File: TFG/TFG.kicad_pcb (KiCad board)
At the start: 2 copper layers, 68.3 x 44.4 mm, 36 parts, among them IC1 MC74VHC1GT14DBVT1G, IC2 AMS1117-5.0, IC3 AMS1117-5.0, J1 Jack-DC, J2 CON-SMA-EDGE-SRP, J3 CON-SMA-EDGE-SRP, Q1 BFP420

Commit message: BOM Uploaded but SRD and Schottky diodes are pending
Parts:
- BFG135A1: footprint Package_TO_SOT_SMD:SOT-223 -> Package_TO_SOT_SMD:SOT-23
- moved BFG135A1 2.37 mm to (72.4, 74.3)
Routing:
- net Net-(BFG135A1-B): track 2.52 -> 7.57 mm
- net Net-(D1-K): track 15.6 -> 16.8 mm
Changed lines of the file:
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@@
 		(tags "capacitor")
 		(property "Reference" "C10"
-			(at 0 -1.43 360)
+			(at 0 -1.43 0)
 			(layer "F.SilkS")
 			(effects
@@
 		)
 		(property "Value" "C"
-			(at 0 1.43 360)
+			(at 0 1.43 0)
 			(layer "F.Fab")
 			(effects
@@
 		)
 		(fp_text user "${REFERENCE}"
-			(at 0 0 360)
+			(at 0 0 0)
 			(layer "F.Fab")
 			(effects
@@
 		(tags "capacitor")
 		(property "Reference" "C11"
-			(at 0 -1.43 360)
+			(at 0 -1.43 0)
 			(layer "F.SilkS")
 			(effects
@@
 		)
 		(property "Value" "0.1u"
-			(at 0 1.43 360)
+			(at 0 1.43 0)
 			(layer "F.Fab")
 			(effects
@@
 		)
 		(fp_text user "${REFERENCE}"
-			(at 0 0 360)
+			(at 0 0 0)
 			(layer "F.Fab")
 			(effects
@@
 		(tags "capacitor tantalum")
 		(property "Reference" "C6"
-			(at 0 -1.75 360)
+			(at 0 -1.75 0)
 			(layer "F.SilkS")
 			(effects
@@
 		)
 		(property "Value" "10u"
-			(at 0 1.75 360)
+			(at 0 1.75 0)
 			(layer "F.Fab")
 			(effects
@@
 		)
 		(fp_text user "${REFERENCE}"
-			(at 0 0 360)
+			(at 0 0 0)
 			(layer "F.Fab")
 			(effects
@@
 		)
 		(fp_text user "${REFERENCE}"
-			(at 0 0 360)
+			(at 0 0 0)
 			(layer "F.Fab")
 			(effects
@@
 		(tags "capacitor")
 		(property "Reference" "C8"
-			(at 0 -1.43 360)
+			(at 0 -1.43 0)
 			(layer "F.SilkS")
 			(effects
@@
 		)
 		(property "Value" "C"
-			(at 0 1.43 360)
+			(at 0 1.43 0)
 			(layer "F.Fab")
 			(effects
@@
 		)
 		(fp_text user "${REFERENCE}"
-			(at 0 0 360)
+			(at 0 0 0)
 			(layer "F.Fab")
 			(effects
@@
 		)
 	)
-	(footprint "Package_TO_SOT_SMD:SOT-223"
+	(footprint "Package_TO_SOT_SMD:SOT-23"
 		(layer "F.Cu")
-		(at 70 74.5)
-		(descr "module CMS SOT223 4 pins")
-		(tags "CMS SOT")
+		(at 72.3625 74.3)
+		(descr "SOT, 3 Pin (https://www.jedec.org/system/files/docs/to-236h.pdf variant AB), generated with kicad-footprint-generator ipc_gullwing_generator.py")
+		(tags "SOT TO_SOT_SMD")
 		(property "Reference" "BFG135A1"
-			(at 0 -4.5 0)
+			(at 0 -2.4 0)
 			(layer "F.SilkS")
 			(effects
@@
 		)
 		(property "Value" "Q_NPN_BCE"
-			(at 0 4.5 0)
+			(at 0 2.4 0)
 			(layer "F.Fab")
 			(effects
@@
 			)
 		)
-		(property "Footprint" "Package_TO_SOT_SMD:SOT-223"
+		(property "Footprint" "Package_TO_SOT_SMD:SOT-23"
 			(at 0 0 0)
 			(unlocked yes)
@@
 		(attr smd)
 		(fp_line
-			(start -1.85 -3.41)
-			(end 1.91 -3.41)
+			(start 0 -1.56)
+			(end -0.65 -1.56)
 			(stroke
 				(width 0.12)
@@
 		)
 		(fp_line
-			(start -1.85 3.41)
-			(end 1.91 3.41)
+			(start 0 -1.56)
+			(end 0.65 -1.56)
 			(stroke
 				(width 0.12)
@@
 		)
 		(fp_line
-			(start 1.91 -3.41)
-			(end 1.91 -2.15)
+			(start 0 1.56)
+			(end -0.65 1.56)
 			(stroke
 				(width 0.12)
@@
 		)
 		(fp_line
-			(start 1.91 3.41)
-			(end 1.91 2.15)
+			(start 0 1.56)
+			(end 0.65 1.56)
 			(stroke
 				(width 0.12)
@@
 		(fp_poly
 			(pts
-				(xy -3.13 -3.31) (xy -3.37 -3.64) (xy -2.89 -3.64) (xy -3.13 -3.31)
+				(xy -1.1625 -1.51) (xy -1.4025 -1.84) (xy -0.9225 -1.84) (xy -1.1625 -1.51)
 			)
 			(stroke
@@
 		)
 		(fp_line
-			(start -4.4 -3.6)
-			(end -4.4 3.6)
+			(start -1.92 -1.7)
+			(end -1.92 1.7)
 			(stroke
 				(width 0.05)
@@
 		)
 		(fp_line
-			(start -4.4 3.6)
-			(end 4.4 3.6)
+			(start -1.92 1.7)
+			(end 1.92 1.7)
 			(stroke
 				(width 0.05)
@@
 		)
 		(fp_line
-			(start 4.4 -3.6)
-			(end -4.4 -3.6)
+			(start 1.92 -1.7)
+			(end -1.92 -1.7)
 			(stroke
 				(width 0.05)
@@
 		)
 		(fp_line
-			(start 4.4 3.6)
-			(end 4.4 -3.6)
+			(start 1.92 1.7)
+			(end 1.92 -1.7)
 			(stroke
 				(width 0.05)
@@
 		)
 		(fp_line
-			(start -1.85 -2.3)
-			(end -1.85 3.35)
+			(start -0.65 -1.125)
+			(end -0.325 -1.45)
 			(stroke
 				(width 0.1)
@@
 		)
 		(fp_line
-			(start -1.85 -2.3)
-			(end -0.8 -3.35)
+			(start -0.65 1.45)
+			(end -0.65 -1.125)
 			(stroke
 				(width 0.1)
@@
 		)
 		(fp_line
-			(start -1.85 3.35)
-			(end 1.85 3.35)
+			(start -0.325 -1.45)
+			(end 0.65 -1.45)
 			(stroke
 				(width 0.1)
@@
 		)
 		(fp_line
-			(start -0.8 -3.35)
-			(end 1.85 -3.35)
+			(start 0.65 -1.45)
+			(end 0.65 1.45)
 			(stroke
 				(width 0.1)
@@
 		)
 		(fp_line
-			(start 1.85 -3.35)
-			(end 1.85 3.35)
+			(start 0.65 1.45)
+			(end -0.65 1.45)
 			(stroke
 				(width 0.1)
@@
 		)
 		(fp_text user "${REFERENCE}"
-			(at 0 0 90)
+			(at 0 0 0)
 			(layer "F.Fab")
 			(effects
 				(font
-					(size 0.8 0.8)
-					(thickness 0.12)
+					(size 0.32 0.32)
+					(thickness 0.05)
 				)
 			)
 		)
 		(pad "1" smd roundrect
-			(at -3.15 0)
-			(size 2 1.5)
+			(at -0.9375 -0.95)
+			(size 1.475 0.6)
 			(layers "F.Cu" "F.Paste" "F.Mask")
 			(roundrect_rratio 0.25)
@@
 		)
 		(pad "2" smd roundrect
-			(at 3.15 0)
-			(size 2 3.8)
+			(at 0.9375 0)
+			(size 1.475 0.6)
 			(layers "F.Cu" "F.Paste" "F.Mask")
 			(roundrect_rratio 0.25)
@@
 		)
 		(pad "3" smd roundrect
-			(at -3.15 -2.3)
-			(size 2 1.5)
-			(layers "F.Cu" "F.Paste" "F.Mask")
-			(roundrect_rratio 0.25)
-			(net 2 "GND")
-			(pinfunction "E")
-			(pintype "passive")
-		)
-		(pad "3" smd roundrect
-			(at -3.15 2.3)
-			(size 2 1.5)
+			(at -0.9375 0.95)
+			(size 1.475 0.6)
 			(layers "F.Cu" "F.Paste" "F.Mask")
 			(roundrect_rratio 0.25)
@@
 			(pintype "passive")
 		)
-		(model "${KICAD8_3DMODEL_DIR}/Package_TO_SOT_SMD.3dshapes/SOT-223.wrl"
+		(model "${KICAD8_3DMODEL_DIR}/Package_TO_SOT_SMD.3dshapes/SOT-23.wrl"
 			(offset
 				(xyz 0 0 0)
@@
 		)
 		(fp_text user "${REFERENCE}"
-			(at 0 0 360)
+			(at 0 0 0)
 			(layer "F.Fab")
 			(effects
@@
 	)
 	(segment
-		(start 66.75 74.6)
-		(end 66.85 74.5)
+		(start 67.1 74.6)
+		(end 64.375 74.6)
 		(width 0.2)
 		(layer "F.Cu")
@@
 	)
 	(segment
-		(start 64.375 74.6)
-		(end 66.75 74.6)
+		(start 71.425 73.35)
+		(end 68.35 73.35)
+		(width 0.2)
+		(layer "F.Cu")
+		(net 1)
+	)
+	(segment
+		(start 68.35 73.35)
+		(end 67.1 74.6)
 		(width 0.2)
 		(layer "F.Cu")
@@
 	)
 	(segment
+		(start 83.5 73.75)
+		(end 83.5 74.9)
+		(width 0.2)
+		(layer "F.Cu")
+		(net 3)
+	)
+	(segment
 		(start 93.95 74.35)
 		(end 94 74.4)
@@
 	)
 	(segment
-		(start 73.35 74.3)
-		(end 73.15 74.5)
-		(width 0.2)
-		(layer "F.Cu")
-		(net 8)
-	)
-	(segment

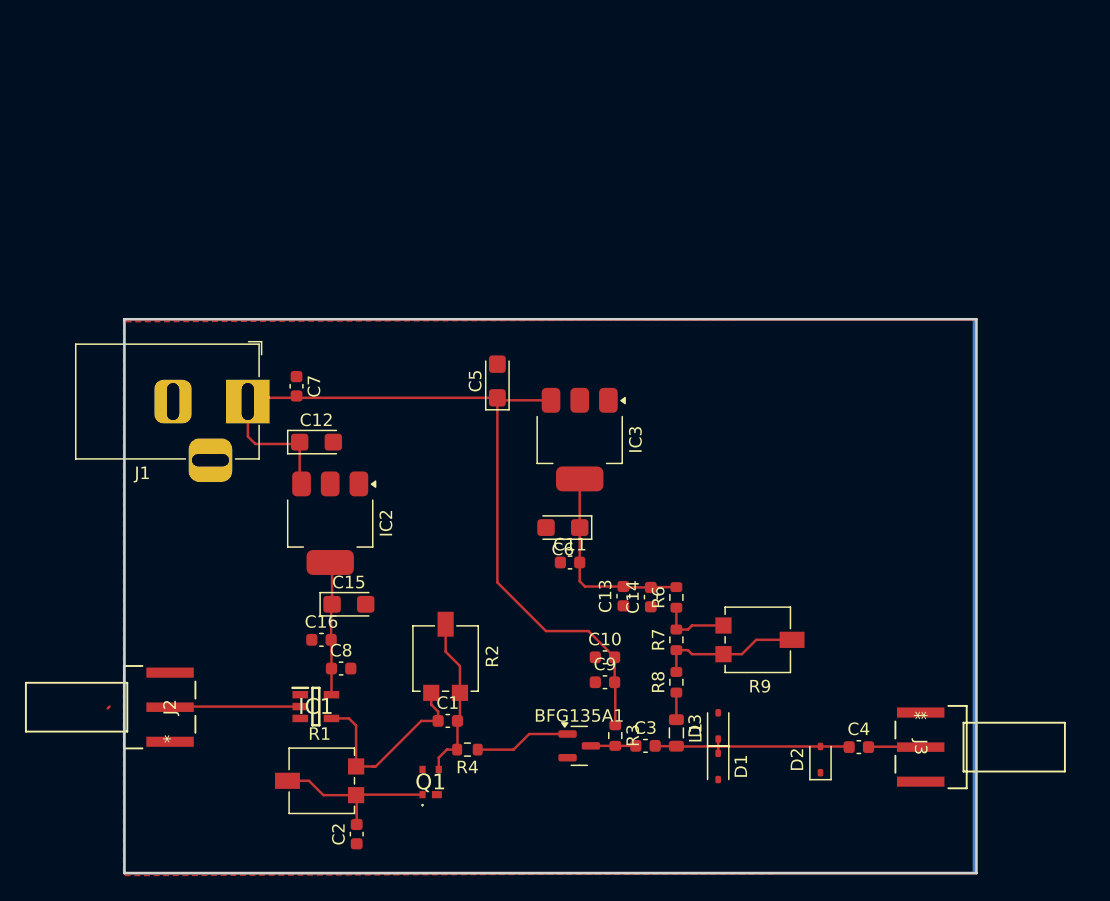
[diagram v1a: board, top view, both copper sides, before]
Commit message: PCB shape as square
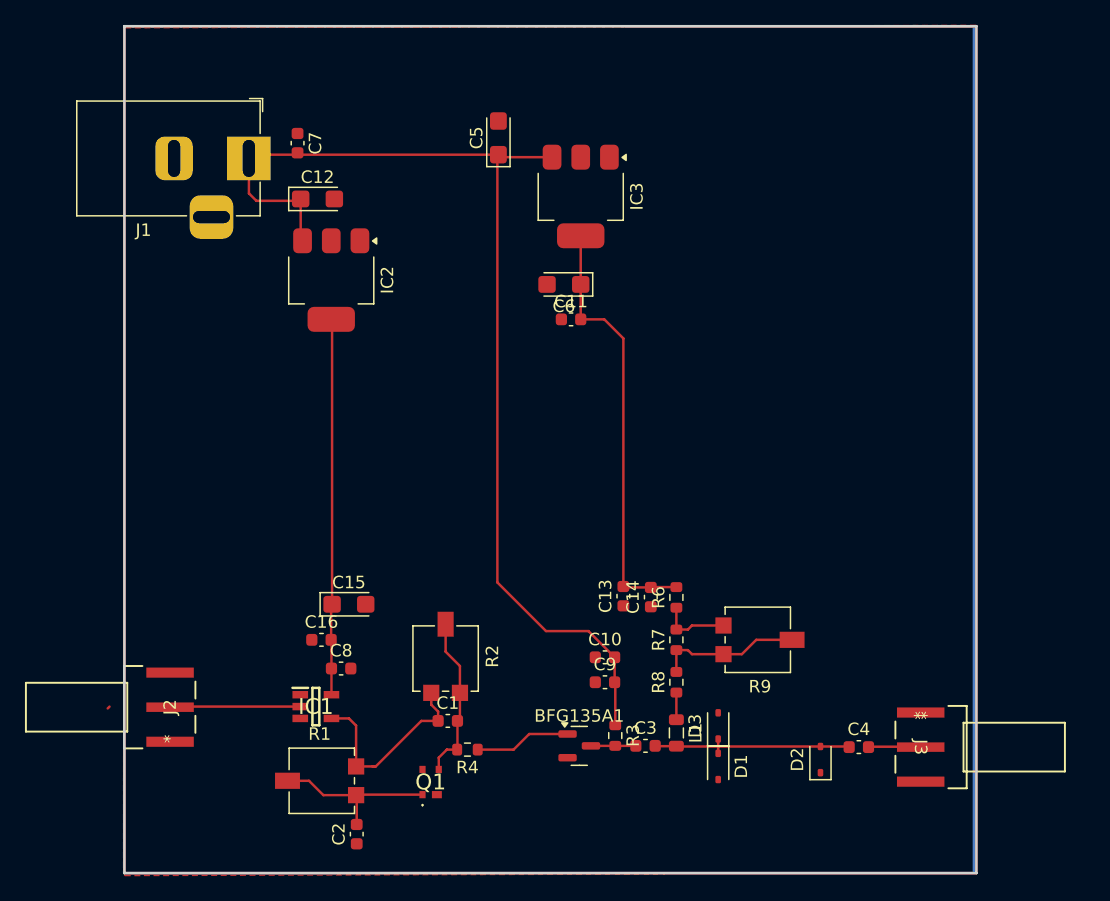
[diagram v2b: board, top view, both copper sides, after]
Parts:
- moved C11 19.5 mm to (71.7, 40.1)
- moved C12 19.5 mm to (51.4, 30.5)
- moved C7 19.5 mm to (49.8, 26.0)
- moved IC2 19.5 mm to (52.5, 37.0)
- moved J1 19.5 mm to (45.9, 27.2)
- moved C5 19.5 mm to (65.9, 25.6)
- moved IC3 19.5 mm to (72.5, 30.3)
- moved C6 19.5 mm to (71.1, 37.3)
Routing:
- net /V5v: track 11.0 -> 30.7 mm
- net /V12v: track 67.8 -> 87.3 mm
- net /V5v_bias: track 16.2 -> 34.9 mm
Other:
- board size 68.3 x 44.4 mm -> 68.3 x 67.9 mm
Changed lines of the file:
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@@
 	(footprint "Capacitor_SMD:C_0603_1608Metric"
 		(layer "F.Cu")
-		(at 71.625 59.6)
+		(at 71.7075 40.11)
 		(descr "Capacitor SMD 0603 (1608 Metric), square (rectangular) end terminal, IPC_7351 nominal, (Body size source: IPC-SM-782 page 76, https://www.pcb-3d.com/wordpress/wp-content/uploads/ipc-sm-782a_amendment_1_and_2.pdf), generated with kicad-footprint-generator")
 		(tags "capacitor")
@@
 	(footprint "Capacitor_Tantalum_SMD:CP_EIA-3216-18_Kemet-A"
 		(layer "F.Cu")
-		(at 71.05 56.8 180)
+		(at 71.1325 37.31 180)
 		(descr "Tantalum Capacitor SMD Kemet-A (3216-18 Metric), IPC_7351 nominal, (Body size from: http://www.kemet.com/Lists/ProductCatalog/Attachments/253/KEM_TC101_STD.pdf), generated with kicad-footprint-generator")
 		(tags "capacitor tantalum")
@@
 	(footprint "Capacitor_Tantalum_SMD:CP_EIA-3216-18_Kemet-A"
 		(layer "F.Cu")
-		(at 65.8 45.05 90)
+		(at 65.8825 25.56 90)
 		(descr "Tantalum Capacitor SMD Kemet-A (3216-18 Metric), IPC_7351 nominal, (Body size from: http://www.kemet.com/Lists/ProductCatalog/Attachments/253/KEM_TC101_STD.pdf), generated with kicad-footprint-generator")
 		(tags "capacitor tantalum")
@@
 	(footprint "Package_TO_SOT_SMD:SOT-223-3_TabPin2"
 		(layer "F.Cu")
-		(at 72.4 49.75 -90)
+		(at 72.4825 30.26 -90)
 		(descr "module CMS SOT223 4 pins")
 		(tags "CMS SOT")
@@
 	(footprint "Connector_BarrelJack:BarrelJack_Horizontal"
 		(layer "F.Cu")
-		(at 45.8 46.7)
+		(at 45.8825 27.21)
 		(descr "DC Barrel Jack")
 		(tags "Power Jack")
@@
 	(footprint "Capacitor_Tantalum_SMD:CP_EIA-3216-18_Kemet-A"
 		(layer "F.Cu")
-		(at 51.3 49.95)
+		(at 51.3825 30.46)
 		(descr "Tantalum Capacitor SMD Kemet-A (3216-18 Metric), IPC_7351 nominal, (Body size from: http://www.kemet.com/Lists/ProductCatalog/Attachments/253/KEM_TC101_STD.pdf), generated with kicad-footprint-generator")
 		(tags "capacitor tantalum")
@@
 	(footprint "Capacitor_SMD:C_0603_1608Metric"
 		(layer "F.Cu")
-		(at 49.7 45.475 -90)
+		(at 49.7825 25.985 -90)
 		(descr "Capacitor SMD 0603 (1608 Metric), square (rectangular) end terminal, IPC_7351 nominal, (Body size source: IPC-SM-782 page 76, https://www.pcb-3d.com/wordpress/wp-content/uploads/ipc-sm-782a_amendment_1_and_2.pdf), generated with kicad-footprint-generator")
 		(tags "capacitor")
@@
 	(footprint "Package_TO_SOT_SMD:SOT-223-3_TabPin2"
 		(layer "F.Cu")
-		(at 52.4 56.45 -90)
+		(at 52.4825 36.96 -90)
 		(descr "module CMS SOT223 4 pins")
 		(tags "CMS SOT")
@@
 	)
 	(gr_rect
-		(start 35.9 40.1)
+		(start 35.9 16.62)
 		(end 104.2 84.5)
 		(stroke
@@
 	)
 	(gr_rect
-		(start 35.9 40.1)
+		(start 35.9 16.64)
 		(end 104 84.5)
 		(stroke
@@
 	)
 	(gr_rect
-		(start 35.9 40.1)
+		(start 35.9 16.61)
 		(end 104.2 84.5)
 		(stroke
@@
 		(layer "F.Cu")
 		(pts
-			(xy 35.929329 40.3) (xy 35.929329 84.7)
+			(xy 35.929329 84.7) (xy 103.929329 84.5)
 		)
 		(height 0.070671)
-		(gr_text "44.4000 mm"
-			(at 34.029329 64.7 90)
+		(gr_text "68.0003 mm"
+			(at 55.700208 88.470671 0.1685165127)
+			(layer "F.Cu")
+			(effects
+				(font
+					(size 1.5 1.5)
+					(thickness 0.3)
+				)
+			)
+		)
+		(format
+			(prefix "")
+			(suffix "")
+			(units 3)
+			(units_format 1)
+			(precision 4)
+		)
+		(style
+			(thickness 0.2)
+			(arrow_length 1.27)
+			(text_position_mode 2)
+			(extension_height 0.58642)
+			(extension_offset 0.5) keep_text_aligned)
+	)
+	(dimension
+		(type aligned)
+		(layer "F.Cu")
+		(pts
+			(xy 35.929121 84.629329) (xy 35.9 16.62)
+		)
+		(height 0.070113)
+		(gr_text "68.0093 mm"
+			(at 32.52 52.81 -89.97546561)
 			(layer "F.Cu")
 			(effects
@@
 	)
 	(segment
-		(start 40.2 46.4)
-		(end 39.8 46)
+		(start 40.2825 26.91)
+		(end 39.8825 26.51)
 		(width 0.2)
 		(layer "F.Cu")
@@
 	)
 	(segment
-		(start 52.55 59.75)
-		(end 52.4 59.6)
+		(start 52.55 62.95)
+		(end 52.55 40.1775)
+		(width 0.2)
+		(layer "F.Cu")
+		(net 4)
+	)
+	(segment
+		(start 52.6325 40.26)
+		(end 52.4825 40.11)
 		(width 0.2)
 		(layer "F.Cu")
@@
 	)
 	(segment
-		(start 52.55 62.95)
-		(end 52.55 59.75)
+		(start 52.55 40.1775)
+		(end 52.4825 40.11)
 		(width 0.2)
 		(layer "F.Cu")
@@
 	)
 	(segment
-		(start 45.8 49.5)
-		(end 46.4 50.1)
+		(start 45.8825 30.01)
+		(end 46.4825 30.61)
 		(width 0.2)
 		(layer "F.Cu")
@@
 	)
 	(segment
-		(start 49.55 46.4)
-		(end 49.7 46.25)
+		(start 65.8 26.9925)
+		(end 65.8 61.2)
 		(width 0.2)
 		(layer "F.Cu")
@@
 	)
 	(segment
-		(start 75.25 72.65)
-		(end 75.25 69.25)
+		(start 49.6325 26.91)
+		(end 49.7825 26.76)
 		(width 0.2)
 		(layer "F.Cu")
@@
 	)
 	(segment
-		(start 49.8 50.1)
-		(end 49.95 49.95)
+		(start 75.25 72.65)
+		(end 75.25 69.25)
 		(width 0.2)
 		(layer "F.Cu")
@@
 	)
 	(segment
-		(start 49.9 50)
-		(end 49.95 49.95)
+		(start 65.8 61.2)
+		(end 69.7 65.1)
 		(width 0.2)
 		(layer "F.Cu")
@@
 	)
 	(segment
-		(start 65.8 46.4)
-		(end 65.8 61.2)
+		(start 49.8825 30.61)
+		(end 50.0325 30.46)
 		(width 0.2)
 		(layer "F.Cu")
@@
 	)
 	(segment
-		(start 66 46.6)
-		(end 65.8 46.4)
+		(start 73.1 65.1)
+		(end 75.2 67.2)
 		(width 0.2)
 		(layer "F.Cu")
@@
 	)
 	(segment
-		(start 65.8 61.2)
-		(end 69.7 65.1)
+		(start 49.9825 30.51)
+		(end 50.0325 30.46)
 		(width 0.2)
 		(layer "F.Cu")
@@
 	)
 	(segment
-		(start 65.8 46.4)
-		(end 45.8 46.4)
+		(start 65.8825 26.91)
+		(end 65.8 26.9925)
 		(width 0.2)
 		(layer "F.Cu")
@@
 	)
 	(segment
-		(start 73.1 65.1)
-		(end 75.2 67.2)
+		(start 66.0825 27.11)
+		(end 65.8825 26.91)
 		(width 0.2)
 		(layer "F.Cu")
@@
 	)
 	(segment
-		(start 69.7 65.1)
-		(end 73.1 65.1)
+		(start 65.8825 26.91)
+		(end 45.8825 26.91)
 		(width 0.2)
 		(layer "F.Cu")
@@
 	)
 	(segment
-		(start 70.1 46.6)
-		(end 66 46.6)
+		(start 70.1825 27.11)
+		(end 66.0825 27.11)
 		(width 0.2)
 		(layer "F.Cu")
@@
 	)
 	(segment
-		(start 49.95 49.95)
-		(end 49.95 53.15)
+		(start 50.0325 30.46)
+		(end 50.0325 33.66)
 		(width 0.2)
 		(layer "F.Cu")
@@
 	)
 	(segment
-		(start 49.95 53.15)
-		(end 50.1 53.3)
+		(start 50.0325 33.66)
+		(end 50.1825 33.81)
 		(width 0.2)
 		(layer "F.Cu")
@@
 	)
 	(segment
-		(start 46.4 50.1)
-		(end 49.8 50.1)
+		(start 46.4825 30.61)
+		(end 49.8825 30.61)
 		(width 0.2)
 		(layer "F.Cu")
@@
 	)
 	(segment
-		(start 45.8 46.4)
-		(end 45.8 49.5)
+		(start 45.8825 26.91)
+		(end 45.8825 30.01)
 		(width 0.2)
 		(layer "F.Cu")
@@
 	)
 	(segment
-		(start 80.15 72.2)
-		(end 80.15 70.025)
+		(start 69.7 65.1)
+		(end 73.1 65.1)
 		(width 0.2)
 		(layer "F.Cu")
-		(net 11)
+		(net 10)
 	)
 	(segment
-		(start 72.4 56.8)
-		(end 72.4 59.6)
+		(start 80.15 72.2)
+		(end 80.15 70.025)
 		(width 0.2)
 		(layer "F.Cu")
-		(net 12)
+		(net 11)
 	)
 	(segment
-		(start 72.4 52.9)
-		(end 72.4 56.8)
+		(start 72.4825 37.31)
+		(end 72.4825 40.11)
 		(width 0.2)
 		(layer "F.Cu")
@@
 	)
 	(segment
-		(start 72.4 59.6)
-		(end 72.4 61.1)
+		(start 72.4825 33.41)
+		(end 72.4825 37.31)
 		(width 0.2)
 		(layer "F.Cu")
@@
 	)
 	(segment
-		(start 72.4 61.1)
-		(end 72.825 61.525)
+		(start 72.4825 40.11)
+		(end 74.37 40.11)
 		(width 0.2)
 		(layer "F.Cu")
@@
 	)
 	(segment
-		(start 75.975 61.6)
+		(start 75.9 41.64)
 		(end 75.9 61.525)
 		(width 0.2)
@@
 	)
 	(segment
-		(start 72.825 61.525)
+		(start 75.975 61.6)
 		(end 75.9 61.525)
 		(width 0.2)
@@
 	)
 	(segment
+		(start 74.37 40.11)
+		(end 75.9 41.64)
+		(width 0.2)
+		(layer "F.Cu")
+		(net 12)
+	)
+	(segment
 		(start 61.1 75.25)
 		(end 61.75 74.6)
@@
 		(min_thickness 0.25)
 		(filled_areas_thickness no)
-		(fill yes
+		(fill
 			(thermal_gap 0.5)
 			(thermal_bridge_width 0.5)
@@
 		(polygon
 			(pts
-				(xy 104.2 40.1) (xy 35.929329 40.3) (xy 35.929329 84.7) (xy 104.2 84.5)
+				(xy 104.17 16.54) (xy 35.899329 16.74) (xy 35.929329 84.7) (xy 104.2 84.5)
 			)
 		)
@@
 		(min_thickness 0.25)
 		(filled_areas_thickness no)
-		(fill yes
+		(fill
 			(thermal_gap 0.5)
 			(thermal_bridge_width 0.5)
@@
 		(polygon
 			(pts
-				(xy 104.2 40.1) (xy 35.829329 40.1) (xy 35.829329 84.5) (xy 104.2 84.5)
+				(xy 104.14 16.56) (xy 35.9 16.64) (xy 35.829329 84.5) (xy 104.2 84.5)
 			)
 		)

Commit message: Power islands and vias placement, only we re missing diodes models
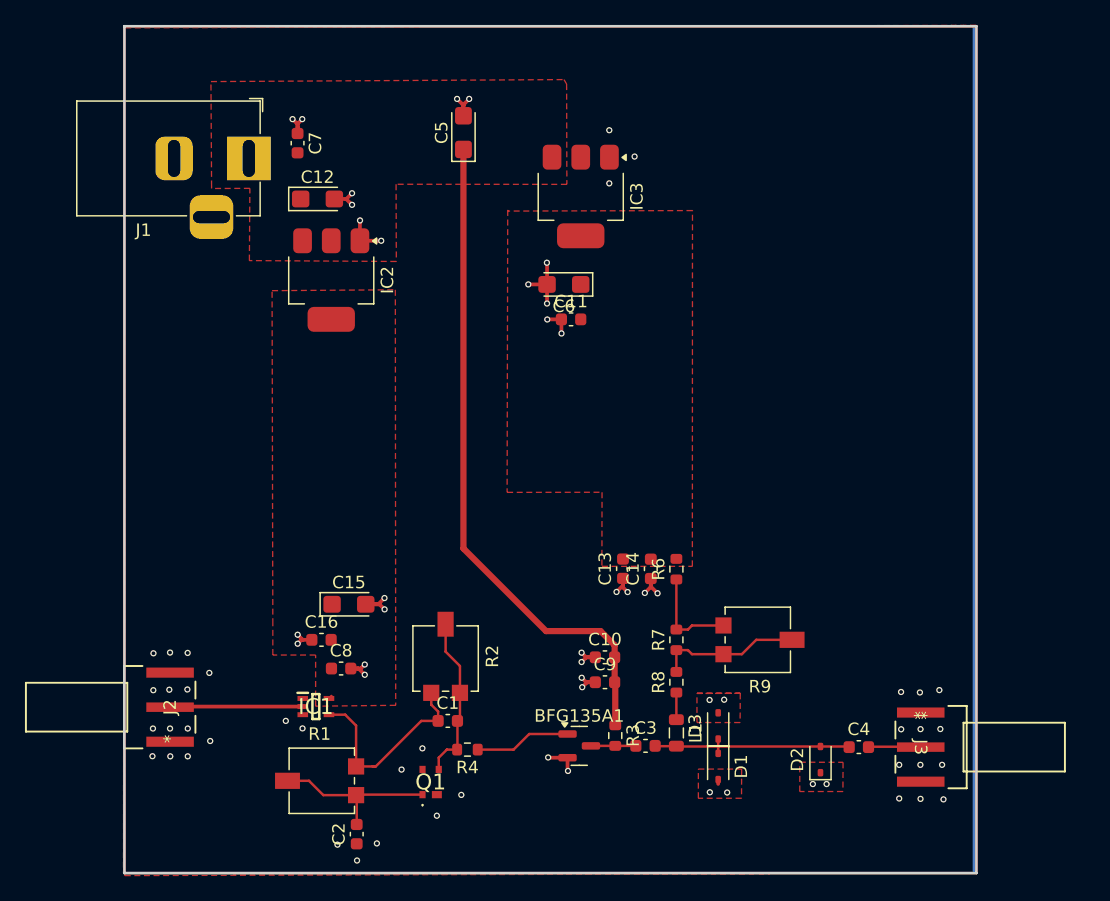
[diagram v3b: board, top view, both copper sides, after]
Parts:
- IC1: footprint MC74VHC1GT14DBVT1G:SOT95P275X110-5N -> MC74VHC1GT04DFT2G:SOT65P210X110-5N
- moved C5 2.83 mm to (63.1, 25.1)
- moved C14 2.27 mm to (78.1, 60.1)
- moved R6 2.27 mm to (80.2, 60.1)
- moved C13 2.20 mm to (75.9, 60.1)
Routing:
- net GND: track 0.57 -> 38.1 mm, vias 0 -> 73
- net /V5v_bias: track 34.9 -> 0.14 mm
- net /V12v: track 87.3 -> 54.0 mm
- net /V5v: track 30.7 -> 1.05 mm
- net Net-(R6-Pad1): track 5.66 -> 7.95 mm
- added copper zone on F.Cu, net /V12v
- added copper zone on F.Cu, net /V5v
- added copper zone on F.Cu, net /V5v_bias
